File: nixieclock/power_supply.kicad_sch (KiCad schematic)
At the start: 31 parts, among them J1 USB_C_Receptacle, Q1 AO3401A, Q2 IRLR3110ZTRPBF, U1 LT3757AEMSE, U2 AMS1117-3.3

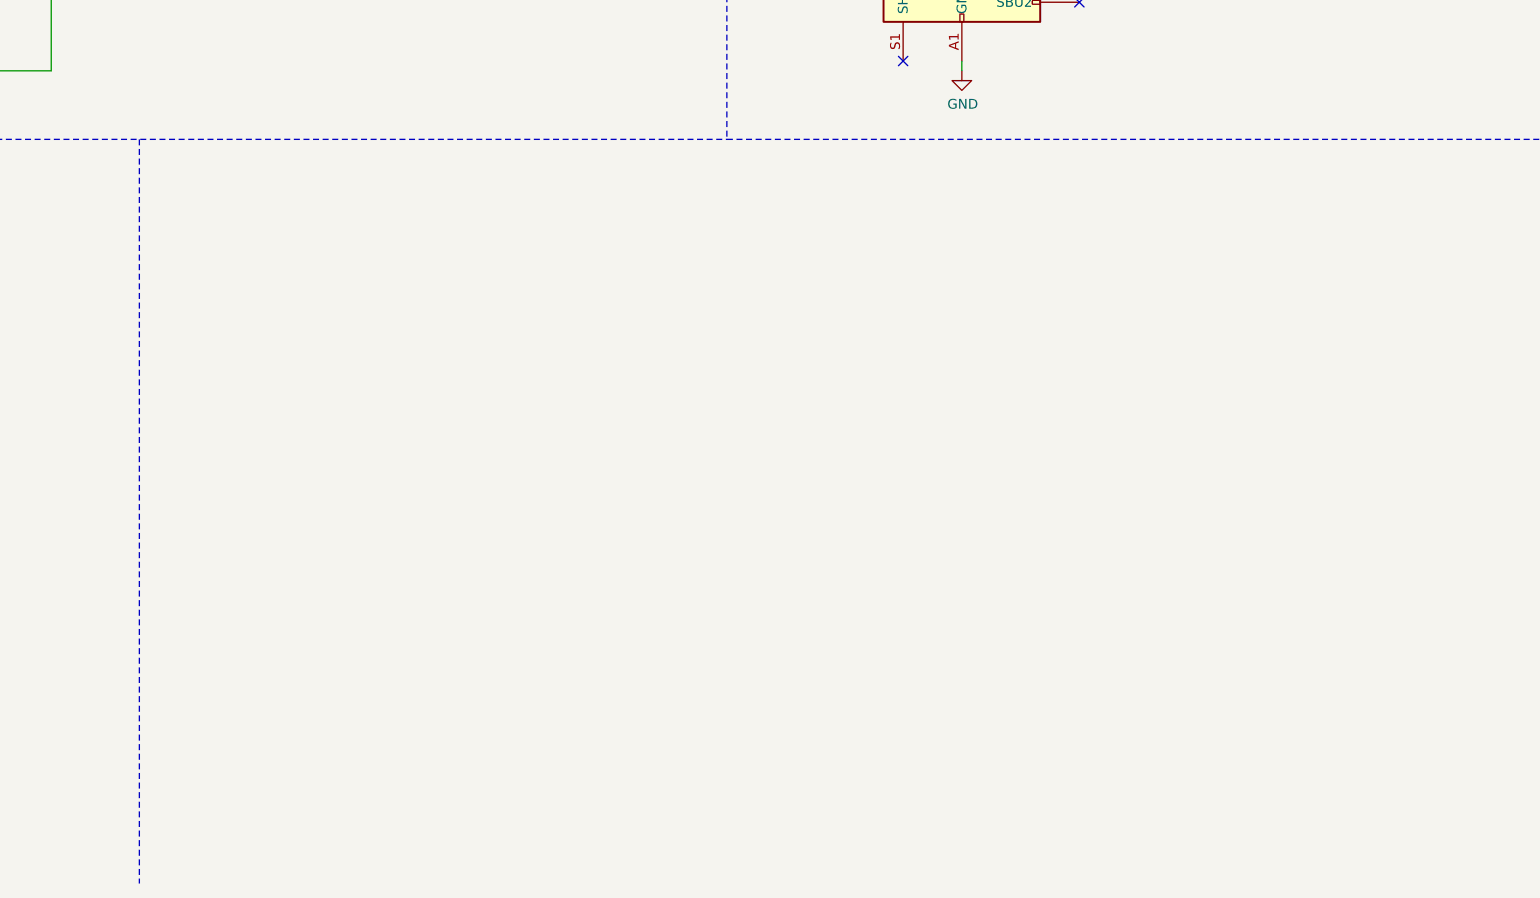
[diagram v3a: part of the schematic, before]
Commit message: finalized neon bulb design (todo: pcb jumpers)
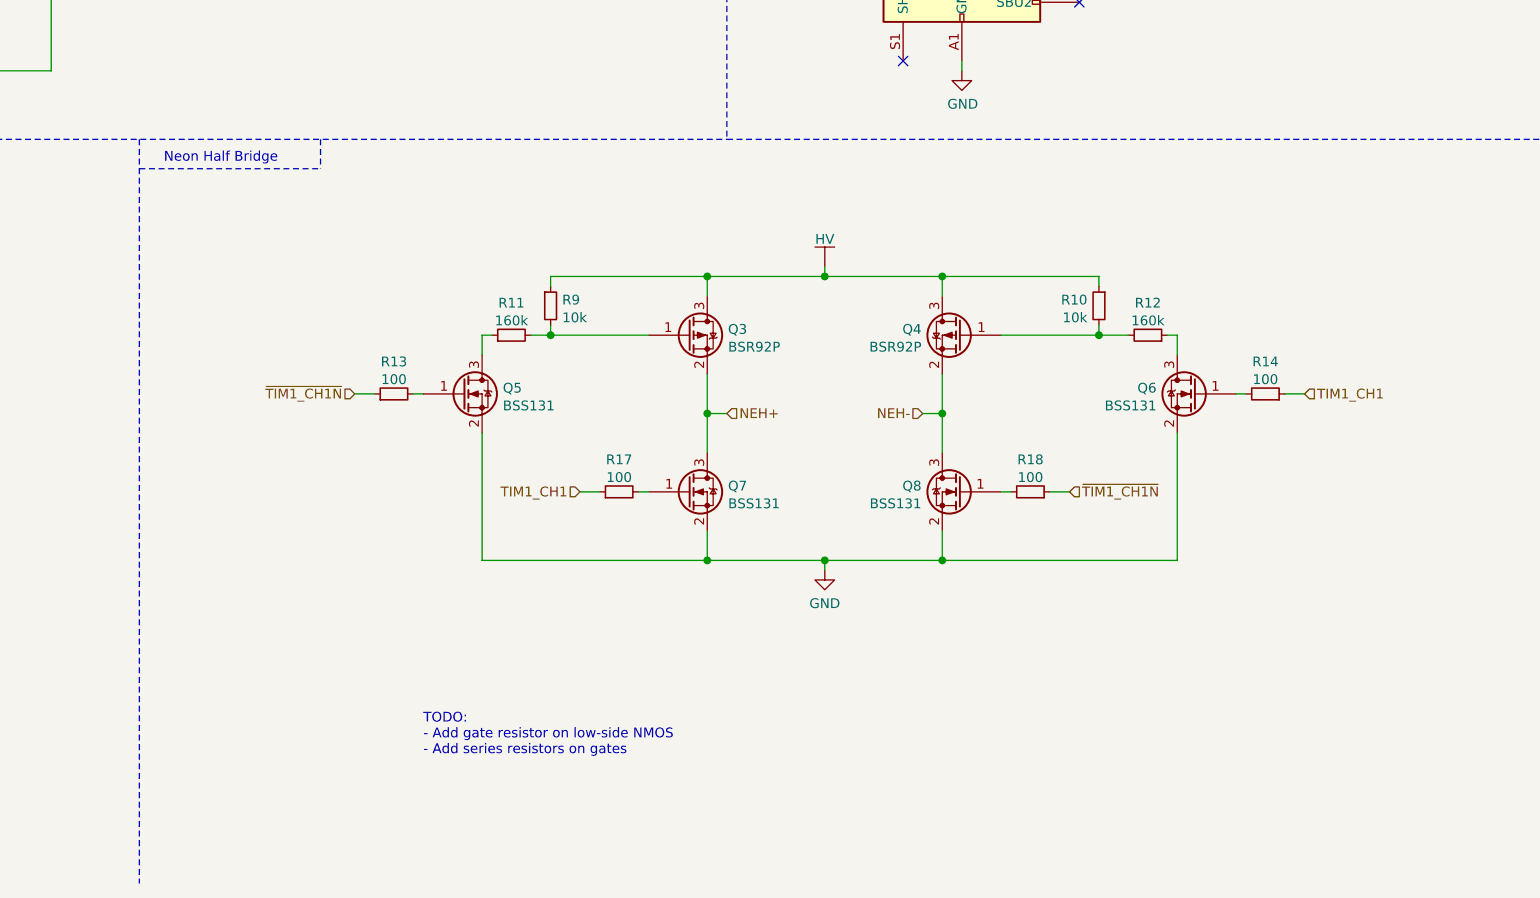
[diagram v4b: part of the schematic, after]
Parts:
- added Q3, Q4: BSR92P, Package_TO_SOT_SMD:SOT-23, symbol Device:Q_PMOS_GSD
- added Q5, Q6, Q7, Q8: BSS131, Package_TO_SOT_SMD:SOT-23, symbol Transistor_FET:BSS138
- added R10, R9: 10k, Resistor_SMD:R_0805_2012Metric_Pad1.15x1.40mm_HandSolder, symbol Device:R_Small
- added R11, R12: 160k, Resistor_SMD:R_0805_2012Metric_Pad1.15x1.40mm_HandSolder, symbol Device:R_Small
- added R13, R14, R17, R18: 100, Resistor_SMD:R_0603_1608Metric_Pad1.05x0.95mm_HandSolder, symbol Device:R_Small
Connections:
- net GND: now also Q5.2 (S), Q6.2 (S), Q7.2 (S), Q8.2 (S)
- net HV: now also Q3.3 (D), Q4.3 (D), R10.1, R9.1
- new net: Q8.1 (G), R18.2
- new net: Q6.1 (G), R14.2
- new net: Q6.3 (D), R12.1
- new net: Q3.1 (G), R11.2, R9.2
- new net: Q7.1 (G), R17.2
- new net: Q4.1 (G), R10.2, R12.2
- new net: Q5.1 (G), R13.2
- new net: Q5.3 (D), R11.1
- new net NEH+: Q3.2 (S), Q7.3 (D)
- new net NEH-: Q4.2 (S), Q8.3 (D)
- new net TIM1_CH1: R14.1, R17.1
- new net ~TIM1_CH1N: R13.1, R18.1
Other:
- note added: "Neon Half Bridge"
- note added: "TODO: - Add gate resistor on low-side NMOS - Add series resistors on gates"

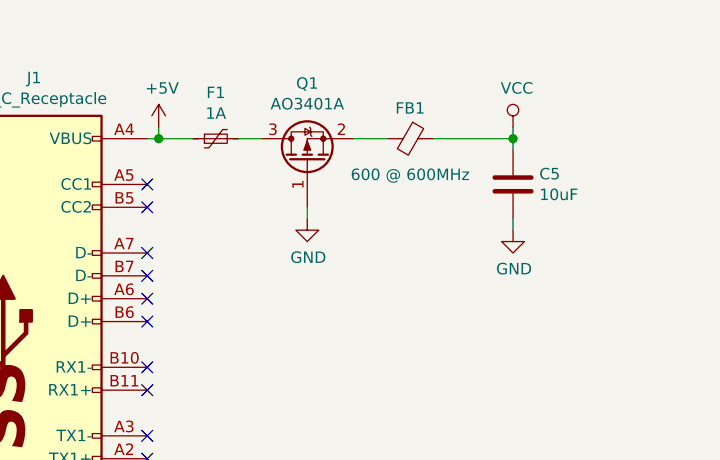
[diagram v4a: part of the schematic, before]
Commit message: finalized layout, added encoder
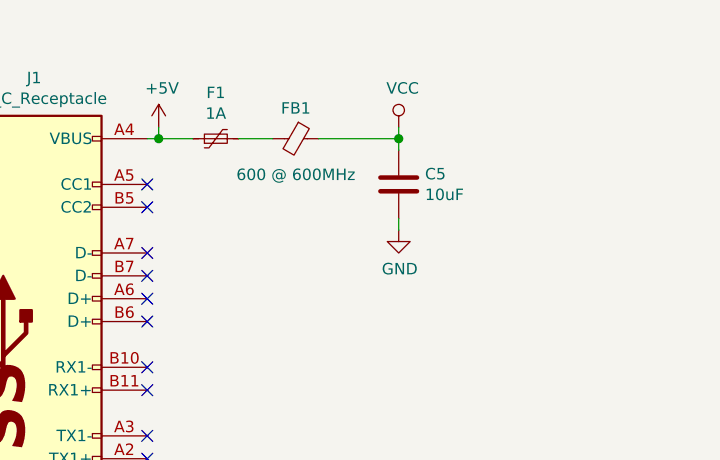
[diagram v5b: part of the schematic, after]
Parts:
- removed Q1: AO3401A, Package_TO_SOT_SMD:SOT-23, symbol Device:Q_PMOS_GSD
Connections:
- net at FB1.2: now also F1.2
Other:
- moved on the sheet: C5, FB1
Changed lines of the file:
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@@
   (junction (at 224.79 25.4) (diameter 1.016) (color 0 0 0 0))
   (junction (at 226.06 127) (diameter 1.016) (color 0 0 0 0))
-  (junction (at 264.16 25.4) (diameter 1.016) (color 0 0 0 0))
+  (junction (at 251.46 25.4) (diameter 1.016) (color 0 0 0 0))
   (no_connect (at 200.66 91.44))
   (no_connect (at 223.52 30.48))
@@
     (stroke (width 0) (type solid) (color 0 0 0 0))
   )
-  (wire (pts (xy 233.68 25.4) (xy 236.22 25.4))
+  (wire (pts (xy 233.68 25.4) (xy 237.49 25.4))
     (stroke (width 0) (type solid) (color 0 0 0 0))
   )
@@
     (stroke (width 0) (type solid) (color 0 0 0 0))
   )
-  (wire (pts (xy 241.3 33.02) (xy 241.3 34.29))
+  (wire (pts (xy 242.57 25.4) (xy 251.46 25.4))
     (stroke (width 0) (type solid) (color 0 0 0 0))
   )
@@
     (stroke (width 0) (type solid) (color 0 0 0 0))
   )
-  (wire (pts (xy 246.38 25.4) (xy 250.19 25.4))
-    (stroke (width 0) (type solid) (color 0 0 0 0))
-  )
   (wire (pts (xy 250.19 134.62) (xy 252.73 134.62))
     (stroke (width 0) (type solid) (color 0 0 0 0))
   )
-  (wire (pts (xy 255.27 25.4) (xy 264.16 25.4))
-    (stroke (width 0) (type solid) (color 0 0 0 0))
-  )
-  (wire (pts (xy 264.16 24.13) (xy 264.16 25.4))
-    (stroke (width 0) (type solid) (color 0 0 0 0))
-  )
-  (wire (pts (xy 264.16 25.4) (xy 264.16 26.67))
-    (stroke (width 0) (type solid) (color 0 0 0 0))
-  )
-  (wire (pts (xy 264.16 34.29) (xy 264.16 35.56))
+  (wire (pts (xy 251.46 24.13) (xy 251.46 25.4))
+    (stroke (width 0) (type solid) (color 0 0 0 0))
+  )
+  (wire (pts (xy 251.46 25.4) (xy 251.46 26.67))
+    (stroke (width 0) (type solid) (color 0 0 0 0))
+  )
+  (wire (pts (xy 251.46 34.29) (xy 251.46 35.56))
     (stroke (width 0) (type solid) (color 0 0 0 0))
   )
@@
     (pin "1")
   )
-  (symbol (lib_id "power:VCC") (at 264.16 24.13 0) (unit 1)
-    (in_bom yes) (on_board yes)
-    (property "Reference" "#PWR04" (id 0) (at 264.16 27.94 0)
-      (effects (font (size 1.27 1.27)) hide)
-    )
-    (property "Value" "VCC" (id 1) (at 264.5918 19.8056 0))
-    (property "Footprint" "" (id 2) (at 264.16 24.13 0)
-      (effects (font (size 1.27 1.27)) hide)
-    )
-    (property "Datasheet" "" (id 3) (at 264.16 24.13 0)
+  (symbol (lib_id "power:VCC") (at 251.46 24.13 0) (unit 1)
+    (in_bom yes) (on_board yes)
+    (property "Reference" "#PWR04" (id 0) (at 251.46 27.94 0)
+      (effects (font (size 1.27 1.27)) hide)
+    )
+    (property "Value" "VCC" (id 1) (at 251.8918 19.8056 0))
+    (property "Footprint" "" (id 2) (at 251.46 24.13 0)
+      (effects (font (size 1.27 1.27)) hide)
+    )
+    (property "Datasheet" "" (id 3) (at 251.46 24.13 0)
       (effects (font (size 1.27 1.27)) hide)
     )
@@
     (pin "1")
   )
-  (symbol (lib_id "power:GND") (at 241.3 34.29 0) (unit 1)
-    (in_bom yes) (on_board yes)
-    (property "Reference" "#PWR06" (id 0) (at 241.3 40.64 0)
-      (effects (font (size 1.27 1.27)) hide)
-    )
-    (property "Value" "GND" (id 1) (at 241.4143 38.6144 0))
-    (property "Footprint" "" (id 2) (at 241.3 34.29 0)
-      (effects (font (size 1.27 1.27)) hide)
-    )
-    (property "Datasheet" "" (id 3) (at 241.3 34.29 0)
-      (effects (font (size 1.27 1.27)) hide)
-    )
-    (pin "1")
-  )
-  (symbol (lib_id "power:GND") (at 264.16 35.56 0) (unit 1)
-    (in_bom yes) (on_board yes)
-    (property "Reference" "#PWR07" (id 0) (at 264.16 41.91 0)
-      (effects (font (size 1.27 1.27)) hide)
-    )
-    (property "Value" "GND" (id 1) (at 264.2743 39.8844 0))
-    (property "Footprint" "" (id 2) (at 264.16 35.56 0)
-      (effects (font (size 1.27 1.27)) hide)
-    )
-    (property "Datasheet" "" (id 3) (at 264.16 35.56 0)
+  (symbol (lib_id "power:GND") (at 251.46 35.56 0) (unit 1)
+    (in_bom yes) (on_board yes)
+    (property "Reference" "#PWR07" (id 0) (at 251.46 41.91 0)
+      (effects (font (size 1.27 1.27)) hide)
+    )
+    (property "Value" "GND" (id 1) (at 251.5743 39.8844 0))
+    (property "Footprint" "" (id 2) (at 251.46 35.56 0)
+      (effects (font (size 1.27 1.27)) hide)
+    )
+    (property "Datasheet" "" (id 3) (at 251.46 35.56 0)
       (effects (font (size 1.27 1.27)) hide)
     )
@@
     (pin "2")
   )
-  (symbol (lib_id "Device:Ferrite_Bead_Small") (at 252.73 25.4 270) (unit 1)
-    (in_bom yes) (on_board yes)
-    (property "Reference" "FB1" (id 0) (at 252.73 22.028 90))
-    (property "Value" "600 @ 600MHz" (id 1) (at 252.73 29.407 90))
-    (property "Footprint" "Inductor_SMD:L_1206_3216Metric_Pad1.42x1.75mm_HandSolder" (id 2) (at 252.73 23.622 90)
-      (effects (font (size 1.27 1.27)) hide)
-    )
-    (property "Datasheet" "~" (id 3) (at 252.73 25.4 0)
+  (symbol (lib_id "Device:Ferrite_Bead_Small") (at 240.03 25.4 270) (unit 1)
+    (in_bom yes) (on_board yes)
+    (property "Reference" "FB1" (id 0) (at 240.03 22.028 90))
+    (property "Value" "600 @ 600MHz" (id 1) (at 240.03 29.407 90))
+    (property "Footprint" "Inductor_SMD:L_1206_3216Metric_Pad1.42x1.75mm_HandSolder" (id 2) (at 240.03 23.622 90)
+      (effects (font (size 1.27 1.27)) hide)
+    )
+    (property "Datasheet" "~" (id 3) (at 240.03 25.4 0)
       (effects (font (size 1.27 1.27)) hide)
     )
@@
     (pin "2")
   )
-  (symbol (lib_id "Device:C") (at 264.16 30.48 0) (unit 1)
-    (in_bom yes) (on_board yes)
-    (property "Reference" "C5" (id 0) (at 267.0811 29.3306 0)
-      (effects (font (size 1.27 1.27)) (justify left))
-    )
-    (property "Value" "10uF" (id 1) (at 267.081 31.629 0)
-      (effects (font (size 1.27 1.27)) (justify left))
-    )
-    (property "Footprint" "Capacitor_SMD:C_1206_3216Metric_Pad1.42x1.75mm_HandSolder" (id 2) (at 265.1252 34.29 0)
-      (effects (font (size 1.27 1.27)) hide)
-    )
-    (property "Datasheet" "~" (id 3) (at 264.16 30.48 0)
+  (symbol (lib_id "Device:C") (at 251.46 30.48 0) (unit 1)
+    (in_bom yes) (on_board yes)
+    (property "Reference" "C5" (id 0) (at 254.3811 29.3306 0)
+      (effects (font (size 1.27 1.27)) (justify left))
+    )
+    (property "Value" "10uF" (id 1) (at 254.381 31.629 0)
+      (effects (font (size 1.27 1.27)) (justify left))
+    )
+    (property "Footprint" "Capacitor_SMD:C_1206_3216Metric_Pad1.42x1.75mm_HandSolder" (id 2) (at 252.4252 34.29 0)
+      (effects (font (size 1.27 1.27)) hide)
+    )
+    (property "Datasheet" "~" (id 3) (at 251.46 30.48 0)
       (effects (font (size 1.27 1.27)) hide)
     )
@@
     )
     (pin "1")
-    (pin "2")
-    (pin "3")
-  )
-  (symbol (lib_id "Device:Q_PMOS_GSD") (at 241.3 27.94 90) (unit 1)
-    (in_bom yes) (on_board yes)
-    (property "Reference" "Q1" (id 0) (at 241.3 19.2594 90))
-    (property "Value" "AO3401A" (id 1) (at 241.3 21.558 90))
-    (property "Footprint" "Package_TO_SOT_SMD:SOT-23" (id 2) (at 238.76 22.86 0)
-      (effects (font (size 1.27 1.27)) hide)
-    )
-    (property "Datasheet" "~" (id 3) (at 241.3 27.94 0)
-      (effects (font (size 1.27 1.27)) hide)
-    )
-    (pin "1")
